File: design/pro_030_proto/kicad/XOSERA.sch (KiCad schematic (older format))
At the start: 42 parts, among them IC15 74HCT245, IC16 74HCT245, IC17 74LS74, IC18 74HCT245, IC19 GAL22V10, IC20 ATF16V8BQL, J10 Upduino_LHS, J11 Upduino_RHS, J12 Conn_01x06_Male, J13 PMOD_TOP, J14 PMOD_BOTTOM, J15 Conn_02x04_Counter_Clockwise, J16 Conn_02x04_Counter_Clockwise, J17 Conn_02x04_Counter_Clockwise, Q1 2N3904

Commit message: Further layout
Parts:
- removed JP16: Jumper, Connector_PinHeader_2.54mm:PinHeader_1x02_P2.54mm_Vertical, symbol Device:Jumper
- renumbered C44 to C43, C45 to C44, C46 to C45, C47 to C46, C48 to C47, C49 to C48, C50 to C49, C51 to C50, C52 to C51, C53 to C52, C54 to C53, IC15 to IC14, IC16 to IC15, IC17 to IC16, IC18 to IC17, IC19 to IC18, IC20 to IC19, JP17 to JP16, JP18 to JP17, R35 to R33, R36 to R34, R37 to R35, R38 to R36, R39 to R37, R40 to R38, R41 to R39, R42 to R40, R43 to R41
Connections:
- net 5V: now also JP15.1; no longer JP15.2
- net UD_5V: now also JP15.2; no longer JP15.1

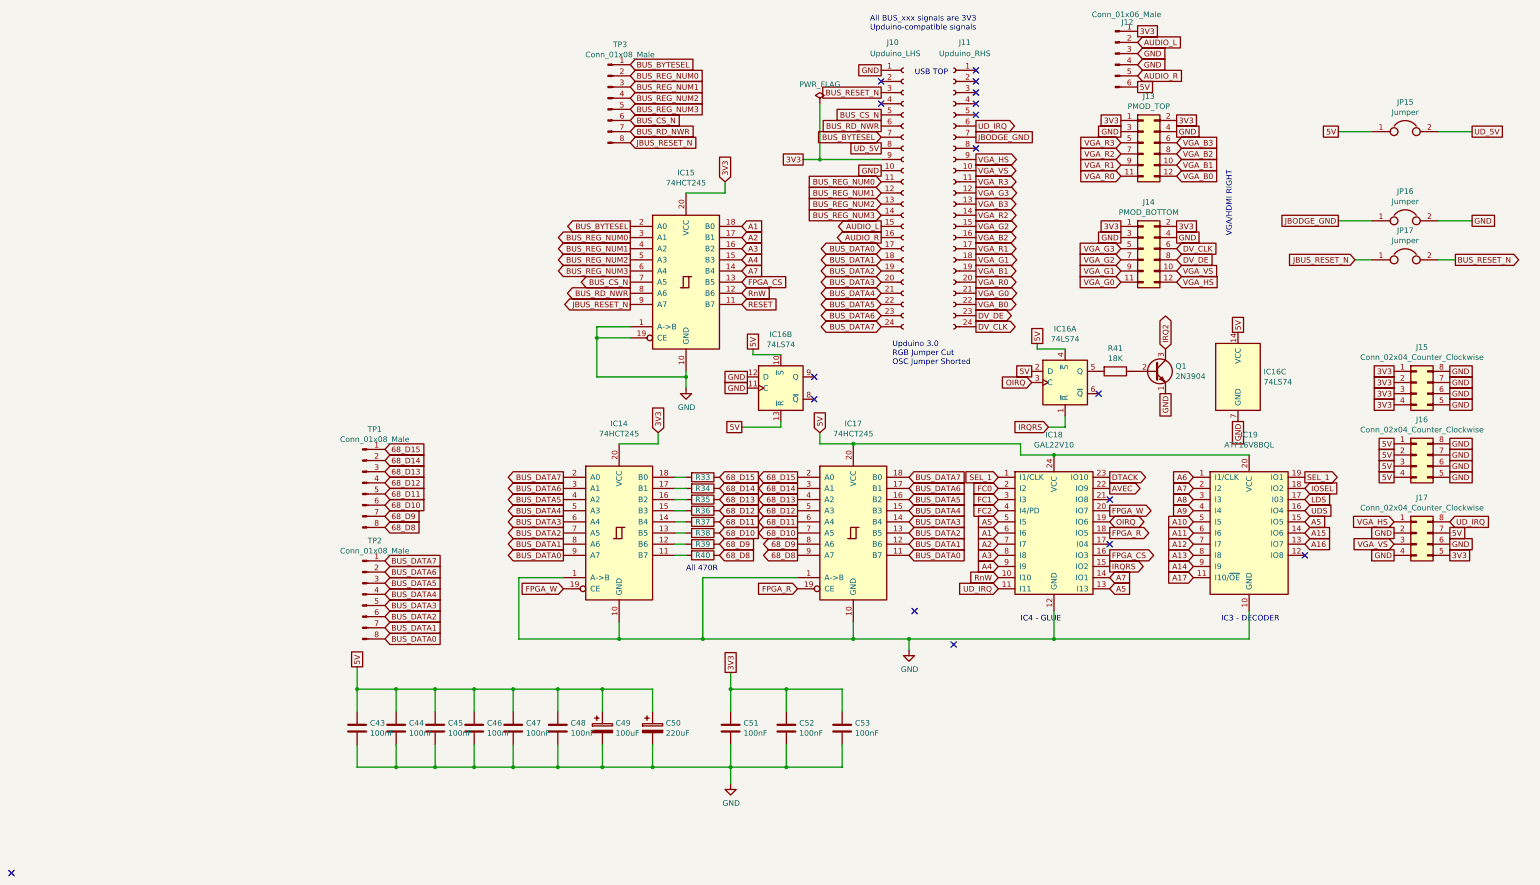
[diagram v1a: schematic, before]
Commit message: Add IO and XVID glue etc.
* Add IO Select glue
* Add Xosera glue
* Add new glues to schematic
* Clean up libs
* Reannotate (again)
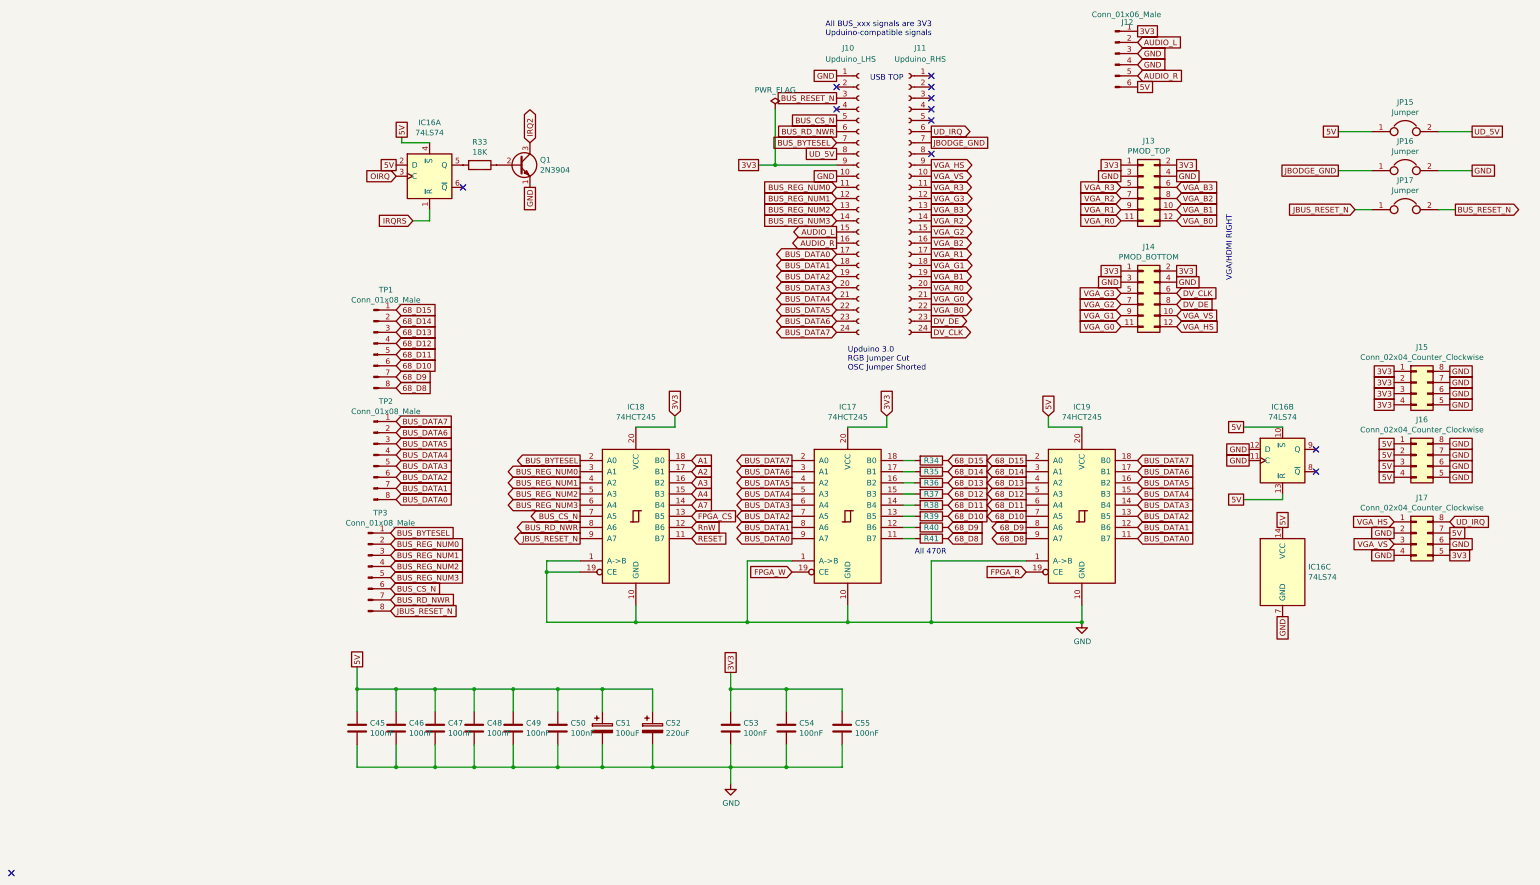
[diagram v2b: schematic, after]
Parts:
- removed IC18: GAL22V10, Package_DIP:DIP-24_W7.62mm_LongPads, symbol rosco_m68k:GAL22V10
- removed IC19: ATF16V8BQL, Package_DIP:DIP-20_W7.62mm_Socket_LongPads, symbol Logic_Programmable:GAL16V8
- renumbered C43 to C45, C44 to C46, C45 to C47, C46 to C48, C47 to C49, C48 to C50, C49 to C51, C50 to C52, C51 to C53, C52 to C54, C53 to C55, IC14 to IC17, IC15 to IC18, IC17 to IC19, R41 to R33, R33 to R34, R34 to R35, R35 to R36, R36 to R37, R37 to R38, R38 to R39, R39 to R40, R40 to R41
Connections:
- no-connect marks 17 -> 12
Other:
- note removed: "IC3 - DECODER"
- note removed: "IC4 - GLUE"
- moved on the sheet: IC16A, IC16B, IC16C, IC17, IC18, IC19, J10, J11, J13, J14, JP16, JP17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

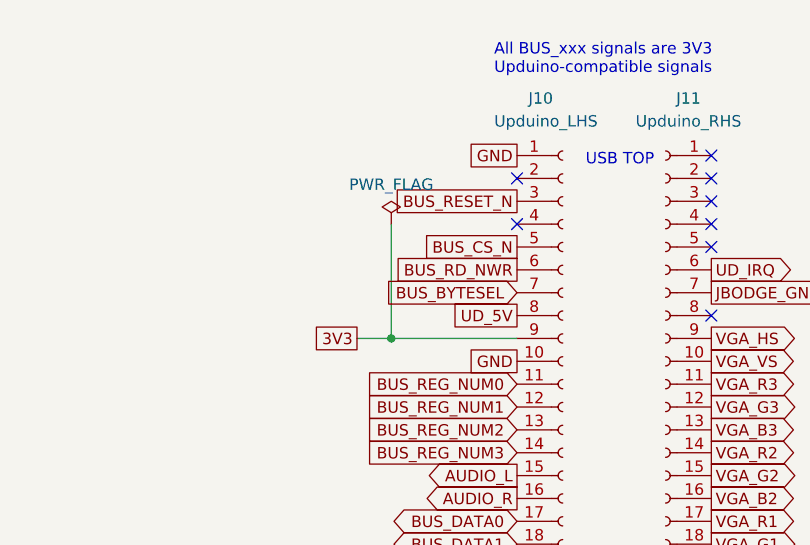
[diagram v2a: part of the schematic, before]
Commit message: Lots of work
* Sort out power and reset circuits, add ATX
* Add PCF8584 and supporting GAL code
* Stub out ATX board outline in PCB
* Various other tidying up and prep for layout
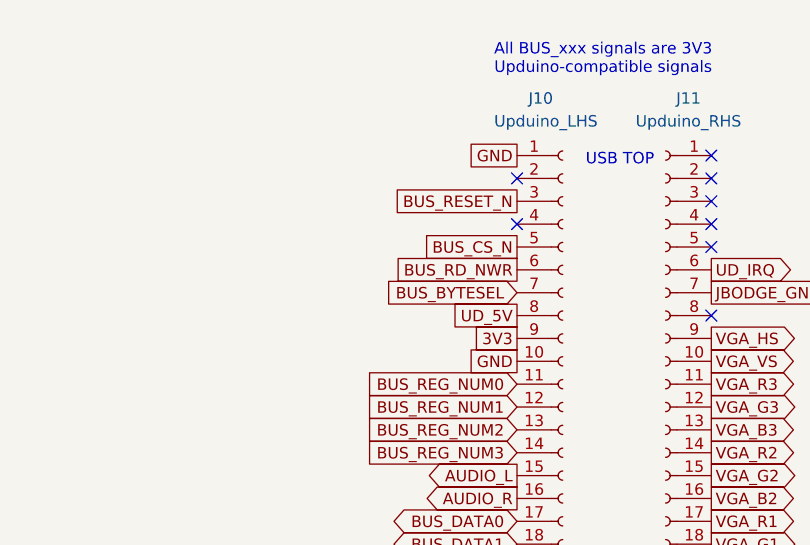
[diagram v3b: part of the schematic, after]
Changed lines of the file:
@@
 $Descr A4 11693 8268
 encoding utf-8
-Sheet 11 13
+Sheet 11 15
 Title "rosco_m68k Pro (030) Prototype"
-Date "2021-07-24"
+Date "2021-10-01"
 Rev "0"
 Comp "The Really Old-School Company Limited"
@@
 Text GLabel 5100 1850 0    50   UnSpc ~ 0
 UD_5V
-Text GLabel 4400 1950 0    50   UnSpc ~ 0
+Text GLabel 5100 1950 0    50   UnSpc ~ 0
 3V3
 Text GLabel 5100 2050 0    50   UnSpc ~ 0
@@
 Text Notes 8650 2400 3    50   ~ 0
 VGA/HDMI RIGHT
-$Comp
-L power:PWR_FLAG #FLG02
-U 1 1 6070D6CE
-P 4550 1450
-F 0 "#FLG02" H 4550 1525 50  0001 C CNN
-F 1 "PWR_FLAG" H 4550 1623 50  0000 C CNN
-F 2 "" H 4550 1450 50  0001 C CNN
-F 3 "~" H 4550 1450 50  0001 C CNN
-	1    4550 1450
-	1    0    0    -1
-$EndComp
-Wire Wire Line
-	4400 1950 4550 1950
-Wire Wire Line
-	4550 1450 4550 1950
-Connection ~ 4550 1950
-Wire Wire Line
-	4550 1950 5100 1950
 Text GLabel 8150 3200 2    50   Input ~ 0
 DV_DE

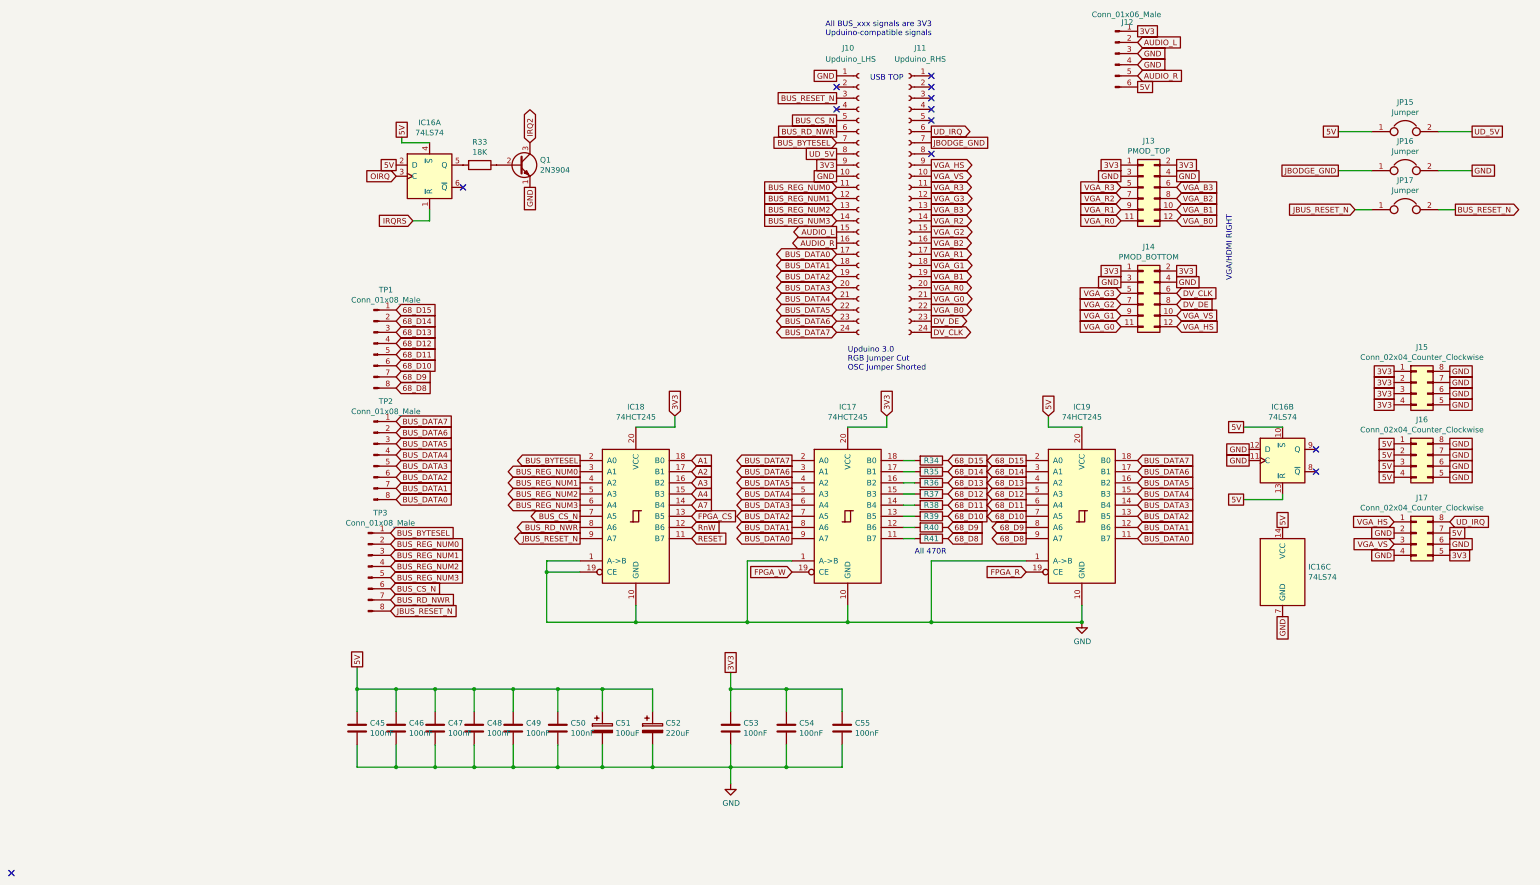
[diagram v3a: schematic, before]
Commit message: First cut placement
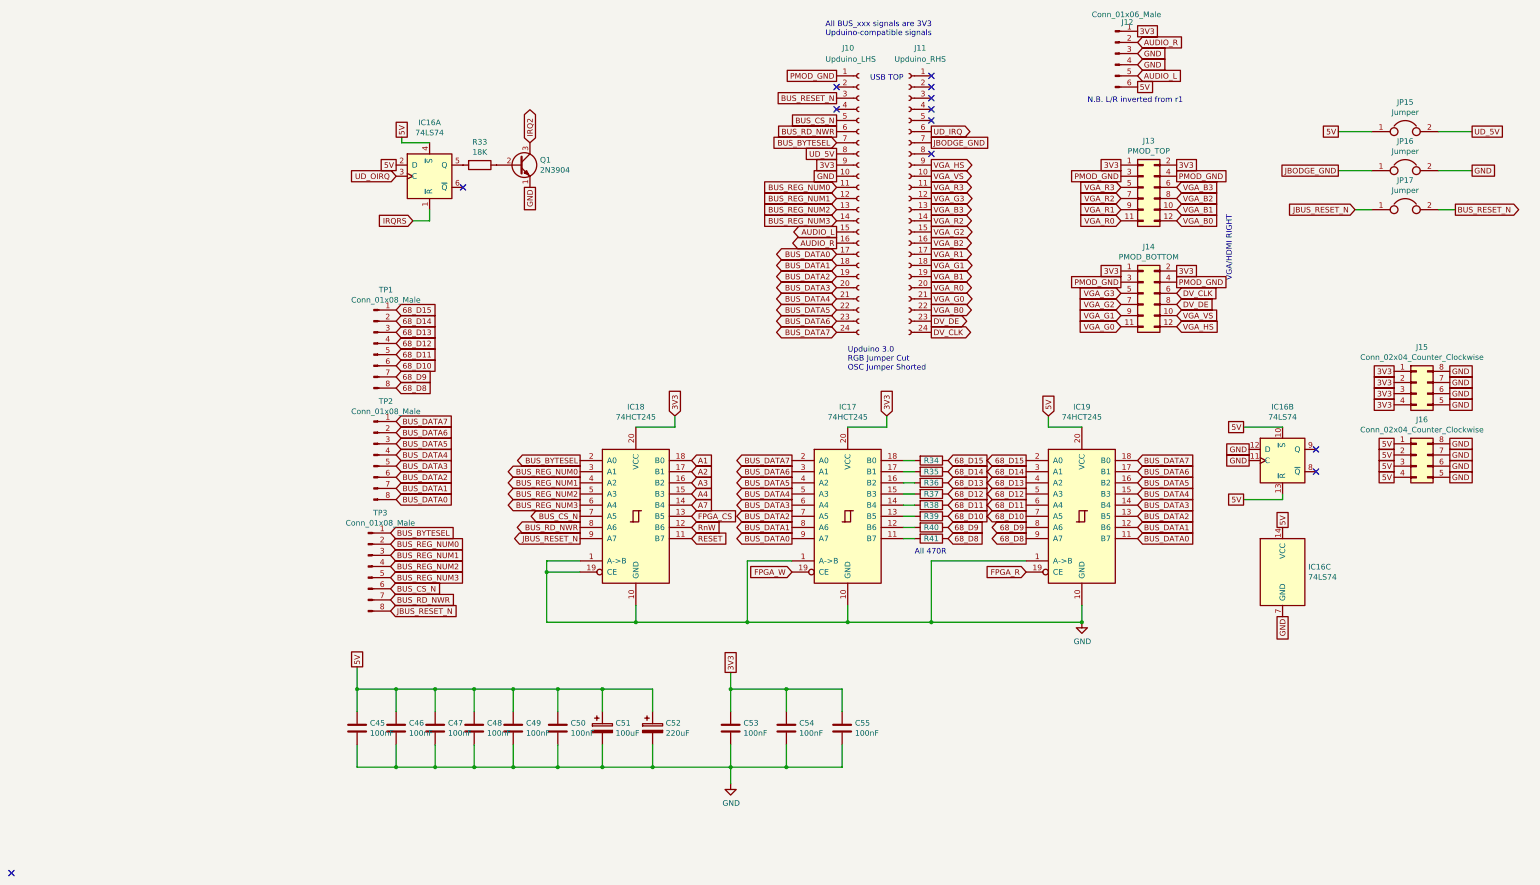
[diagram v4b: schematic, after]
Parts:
- removed J17: Conn_02x04_Counter_Clockwise, Connector_PinHeader_2.54mm:PinHeader_2x04_P2.54mm_Vertical, symbol Connector_Generic:Conn_02x04_Counter_Clockwise
- C45, C46, C47, C48, C49, C50, C53, C54, C55: footprint rosco_m68k:C2.5-3 -> Capacitor_THT:C_Rect_L4.0mm_W2.5mm_P2.50mm
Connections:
- net AUDIO_L: now also J12.5 (Pin_5); no longer J12.2 (Pin_2)
- net AUDIO_R: now also J12.2 (Pin_2); no longer J12.5 (Pin_5)
- net GND: no longer J10.1 (Pin_1), J13.3 (Pin_3), J13.4 (Pin_4), J14.3 (Pin_3), J14.4 (Pin_4)
- net OIRQ renamed UD_OIRQ
- new net PMOD_GND: J10.1 (Pin_1), J13.3 (Pin_3), J13.4 (Pin_4), J14.3 (Pin_3), J14.4 (Pin_4)
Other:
- note added: "N.B. L/R inverted from r1"
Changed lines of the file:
@@
 F 0 "C49" H 2315 7046 50  0000 L CNN
 F 1 "100nF" H 2315 6955 50  0000 L CNN
-F 2 "rosco_m68k:C2.5-3" H 2238 6850 50  0001 C CNN
+F 2 "Capacitor_THT:C_Rect_L4.0mm_W2.5mm_P2.50mm" H 2238 6850 50  0001 C CNN
 F 3 "~" H 2200 7000 50  0001 C CNN
 	1    2200 7000
@@
 F 0 "C53" H 4265 7046 50  0000 L CNN
 F 1 "100nF" H 4265 6955 50  0000 L CNN
-F 2 "rosco_m68k:C2.5-3" H 4188 6850 50  0001 C CNN
+F 2 "Capacitor_THT:C_Rect_L4.0mm_W2.5mm_P2.50mm" H 4188 6850 50  0001 C CNN
 F 3 "~" H 4150 7000 50  0001 C CNN
 	1    4150 7000
@@
 F 0 "C48" H 1965 7046 50  0000 L CNN
 F 1 "100nF" H 1965 6955 50  0000 L CNN
-F 2 "rosco_m68k:C2.5-3" H 1888 6850 50  0001 C CNN
+F 2 "Capacitor_THT:C_Rect_L4.0mm_W2.5mm_P2.50mm" H 1888 6850 50  0001 C CNN
 F 3 "~" H 1850 7000 50  0001 C CNN
 	1    1850 7000
@@
 F 0 "C47" H 1615 7046 50  0000 L CNN
 F 1 "100nF" H 1615 6955 50  0000 L CNN
-F 2 "rosco_m68k:C2.5-3" H 1538 6850 50  0001 C CNN
+F 2 "Capacitor_THT:C_Rect_L4.0mm_W2.5mm_P2.50mm" H 1538 6850 50  0001 C CNN
 F 3 "~" H 1500 7000 50  0001 C CNN
 	1    1500 7000
@@
 F 0 "C46" H 1265 7046 50  0000 L CNN
 F 1 "100nF" H 1265 6955 50  0000 L CNN
-F 2 "rosco_m68k:C2.5-3" H 1188 6850 50  0001 C CNN
+F 2 "Capacitor_THT:C_Rect_L4.0mm_W2.5mm_P2.50mm" H 1188 6850 50  0001 C CNN
 F 3 "~" H 1150 7000 50  0001 C CNN
 	1    1150 7000
@@
 F 0 "C45" H 915 7046 50  0000 L CNN
 F 1 "100nF" H 915 6955 50  0000 L CNN
-F 2 "rosco_m68k:C2.5-3" H 838 6850 50  0001 C CNN
+F 2 "Capacitor_THT:C_Rect_L4.0mm_W2.5mm_P2.50mm" H 838 6850 50  0001 C CNN
 F 3 "~" H 800 7000 50  0001 C CNN
 	1    800  7000
@@
 NoConn ~ 5100 1450
 Text GLabel 5100 1150 0    50   UnSpc ~ 0
-GND
+PMOD_GND
 Text GLabel 5100 1350 0    50   UnSpc ~ 0
 BUS_RESET_N
@@
 VGA_B3
 Text GLabel 7650 2050 0    50   UnSpc ~ 0
-GND
+PMOD_GND
 Text GLabel 7650 1950 0    50   UnSpc ~ 0
 3V3
@@
 VGA_VS
 Text GLabel 7650 3000 0    50   UnSpc ~ 0
-GND
+PMOD_GND
 Text GLabel 7650 2900 0    50   UnSpc ~ 0
 3V3
@@
 VGA_G3
 Text GLabel 8150 2050 2    50   UnSpc ~ 0
-GND
+PMOD_GND
 Text GLabel 8150 1950 2    50   UnSpc ~ 0
 3V3
 Text GLabel 8150 3000 2    50   UnSpc ~ 0
-GND
+PMOD_GND
 Text GLabel 8150 2900 2    50   UnSpc ~ 0
 3V3
@@
 	1    0    0    -1
 $EndComp
-$Comp
-L Connector_Generic:Conn_02x04_Counter_Clockwise J17
-U 1 1 6071C4F2
-P 10300 5250
-F 0 "J17" H 10350 5567 50  0000 C CNN
-F 1 "Conn_02x04_Counter_Clockwise" H 10350 5476 50  0000 C CNN
-F 2 "Connector_PinHeader_2.54mm:PinHeader_2x04_P2.54mm_Vertical" H 10300 5250 50  0001 C CNN
-F 3 "~" H 10300 5250 50  0001 C CNN
-	1    10300 5250
-	1    0    0    -1
-$EndComp
 Text GLabel 10100 3800 0    50   UnSpc ~ 0
 3V3
@@
 Text GLabel 10100 4750 0    50   UnSpc ~ 0
 5V
-Text GLabel 10100 5150 0    50   Input ~ 0
-VGA_HS
-Text GLabel 10100 5350 0    50   Input ~ 0
-VGA_VS
-Text GLabel 10100 5250 0    50   UnSpc ~ 0
-GND
-Text GLabel 10100 5450 0    50   UnSpc ~ 0
-GND
-Text GLabel 10600 5250 2    50   UnSpc ~ 0
-5V
-Text GLabel 10600 5350 2    50   UnSpc ~ 0
-GND
-Text GLabel 10600 5450 2    50   UnSpc ~ 0
-3V3
 $Comp
 L Device:C C54
@@
 F 0 "C54" H 4765 7046 50  0000 L CNN
 F 1 "100nF" H 4765 6955 50  0000 L CNN
-F 2 "rosco_m68k:C2.5-3" H 4688 6850 50  0001 C CNN
+F 2 "Capacitor_THT:C_Rect_L4.0mm_W2.5mm_P2.50mm" H 4688 6850 50  0001 C CNN
 F 3 "~" H 4650 7000 50  0001 C CNN
 	1    4650 7000
@@
 F 0 "C55" H 5265 7046 50  0000 L CNN
 F 1 "100nF" H 5265 6955 50  0000 L CNN
-F 2 "rosco_m68k:C2.5-3" H 5188 6850 50  0001 C CNN
+F 2 "Capacitor_THT:C_Rect_L4.0mm_W2.5mm_P2.50mm" H 5188 6850 50  0001 C CNN
 F 3 "~" H 5150 7000 50  0001 C CNN
 	1    5150 7000
@@
 F 0 "C50" H 2715 7046 50  0000 L CNN
 F 1 "100nF" H 2715 6955 50  0000 L CNN
-F 2 "rosco_m68k:C2.5-3" H 2638 6850 50  0001 C CNN
+F 2 "Capacitor_THT:C_Rect_L4.0mm_W2.5mm_P2.50mm" H 2638 6850 50  0001 C CNN
 F 3 "~" H 2600 7000 50  0001 C CNN
 	1    2600 7000
@@
 5V
 Text GLabel 1150 2050 0    50   Input ~ 0
-OIRQ
+UD_OIRQ
 NoConn ~ 1750 2150
 Text GLabel 1300 2450 0    50   Input ~ 0
@@
 Text GLabel 7800 950  2    50   Input ~ 0
 GND
+Text GLabel 7800 850  2    50   Input ~ 0
+AUDIO_R
 Text GLabel 7800 1150 2    50   Input ~ 0
-AUDIO_R
-Text GLabel 7800 850  2    50   Input ~ 0
 AUDIO_L
 $Comp
@@
 Text GLabel 7800 1250 2    50   UnSpc ~ 0
 5V
-Text GLabel 10600 5150 2    50   Input ~ 0
-UD_IRQ
 Wire Wire Line
 	10500 1650 10800 1650
@@
 	1    0    0    -1
 $EndComp
+Text Notes 7350 1400 0    50   ~ 0
+N.B. L/R inverted from r1
 $EndSCHEMATC

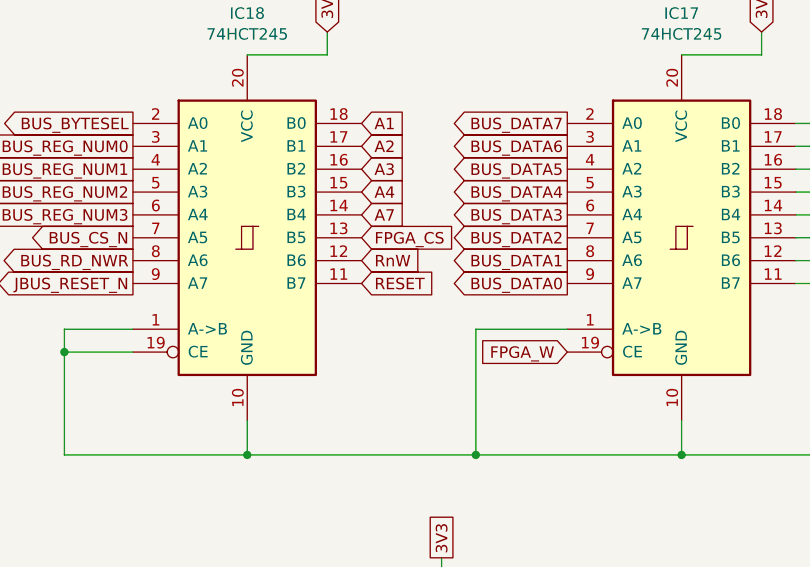
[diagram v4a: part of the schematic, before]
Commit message: Replace 7493s and 7404 with IC10 GAL
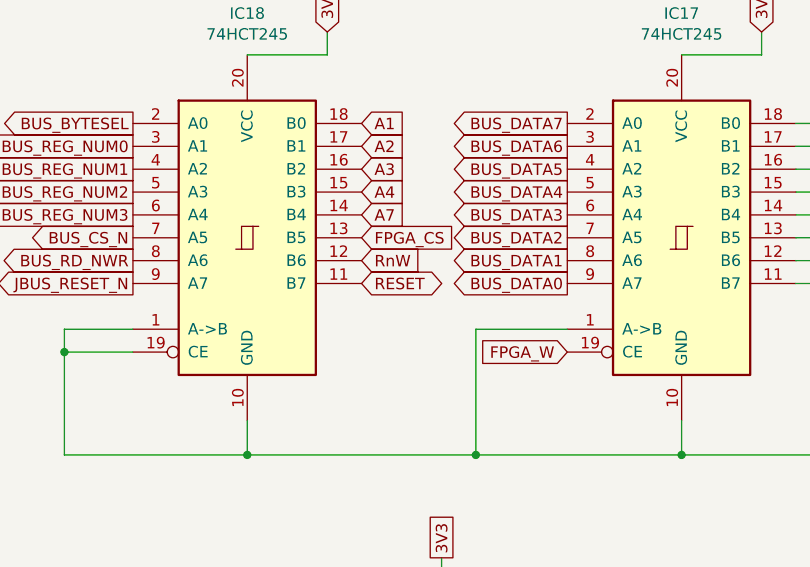
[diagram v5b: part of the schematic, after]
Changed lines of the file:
@@
 Text GLabel 3650 4200 1    50   Input ~ 0
 3V3
-Text GLabel 3800 5300 2    50   Input ~ 0
+Text GLabel 3800 5300 2    50   3State ~ 0
 RESET
 Wire Wire Line
